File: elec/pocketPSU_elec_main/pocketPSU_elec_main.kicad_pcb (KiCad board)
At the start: 2 copper layers, 90 x 90 mm, 96 parts, among them J1 Header-Male-2.54_1x20, J2 Screw_Terminal_01x02, J3 Conn_01x12_Pin, J4 Screw_Terminal_01x02, J5 SM04B-GHS-TB(LF)(SN), Q1 2N7002_C5224215, SW1 EC11E09244BS, U2 ESP32-S3-WROOM-1(N16R2), U3 AMS1117-3.3, U4 FUSB302MPX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

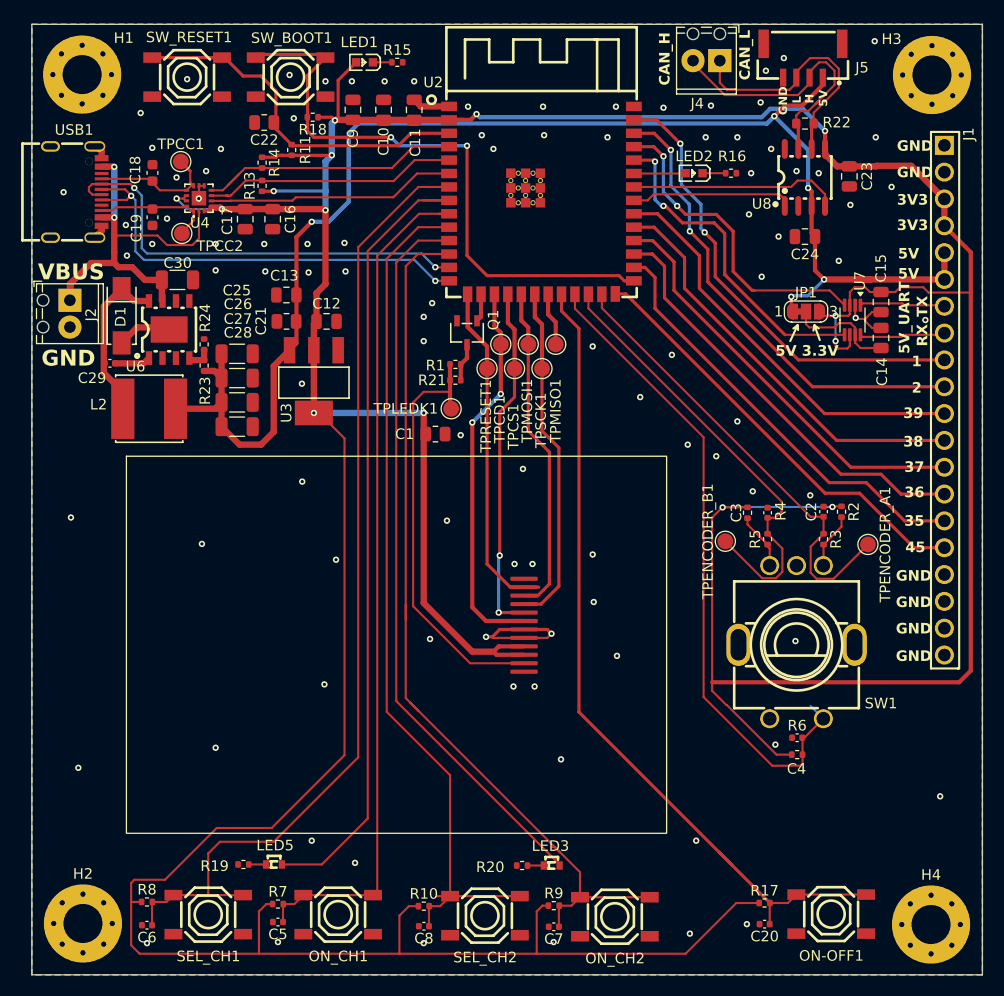
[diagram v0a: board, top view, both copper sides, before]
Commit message: fix pcb drc
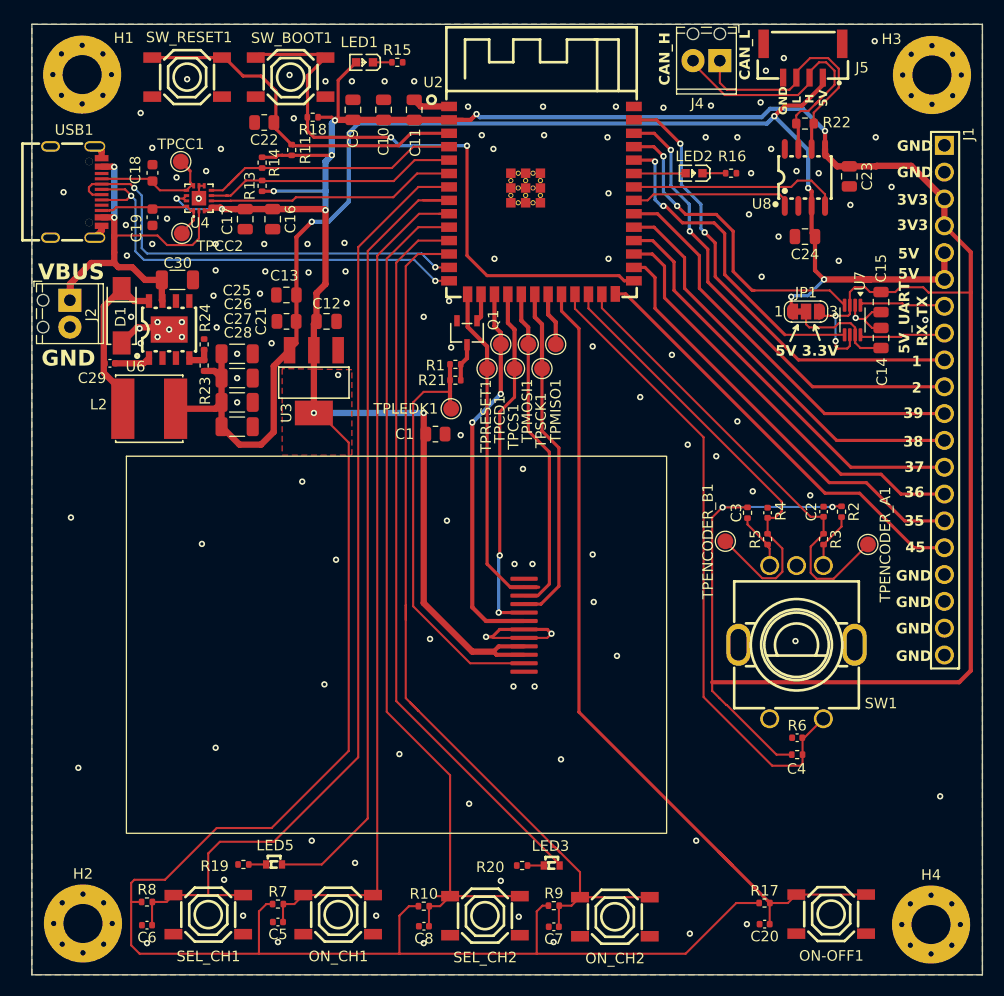
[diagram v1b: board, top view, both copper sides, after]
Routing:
- net /microcontroller/ENCODER_BT: track 62.2 -> 60.5 mm
- net GND: vias 99 -> 124
- added copper zone on F.Cu, net +3.3V

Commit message: add silk githash string
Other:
- board text added: "pocketPSU ${git_hash}"
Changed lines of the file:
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@@
+		)
+	)
+	(gr_text "pocketPSU ${git_hash}"
+		(at 101 112.4 90)
+		(layer "F.SilkS")
+		(effects
+			(font
+				(size 1.5 1.5)
+				(thickness 0.3)
+				(bold yes)
+			)
+			(justify left bottom)
 		)
 	)

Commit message: add silk tag string
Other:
- board text added: "pocketPSU ${git_tag}"
- board text removed: "pocketPSU ${git_hash}"
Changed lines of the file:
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@@
 		)
 	)
-	(gr_text "pocketPSU ${git_hash}"
+	(gr_text "pocketPSU ${git_tag}"
 		(at 101 112.4 90)
 		(layer "F.SilkS")
